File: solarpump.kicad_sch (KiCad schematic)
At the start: 16 parts, among them J1 8-way_Screw, J2 UART_IO, J3 AUX_POWER, J4 USB_A, J5 Conn_DISP, J6 Conn_DISP

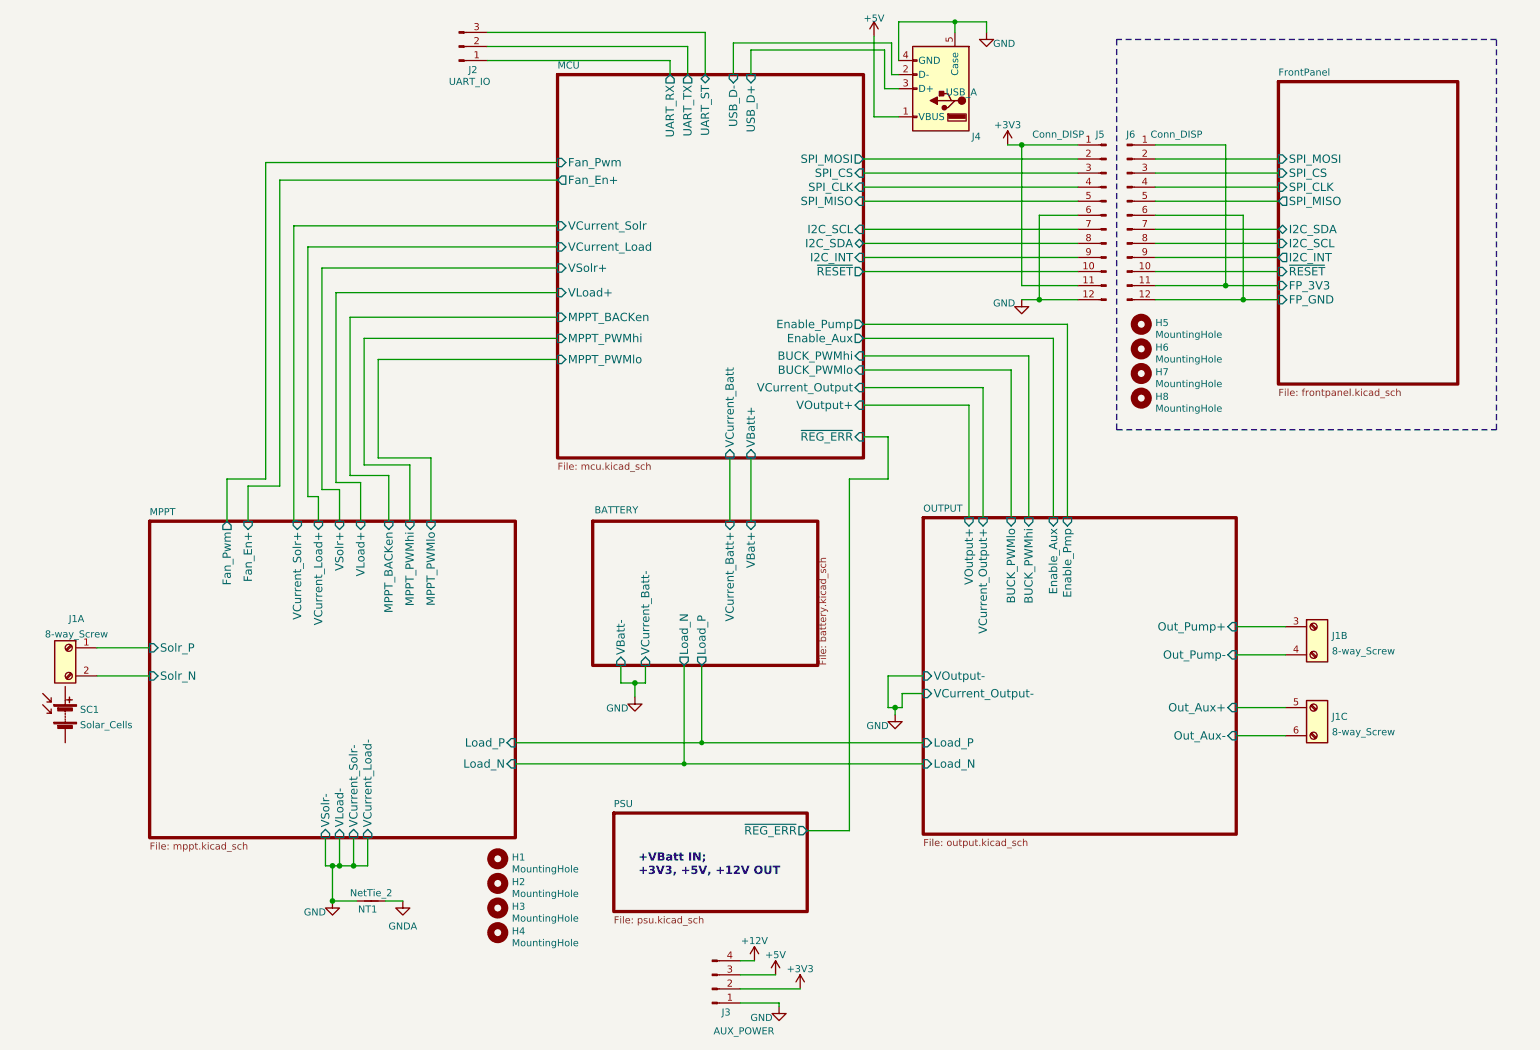
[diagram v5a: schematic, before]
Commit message: Rework with larger display; update component selection; add SWD conn; add RTC chip and QWIIC i2c socket
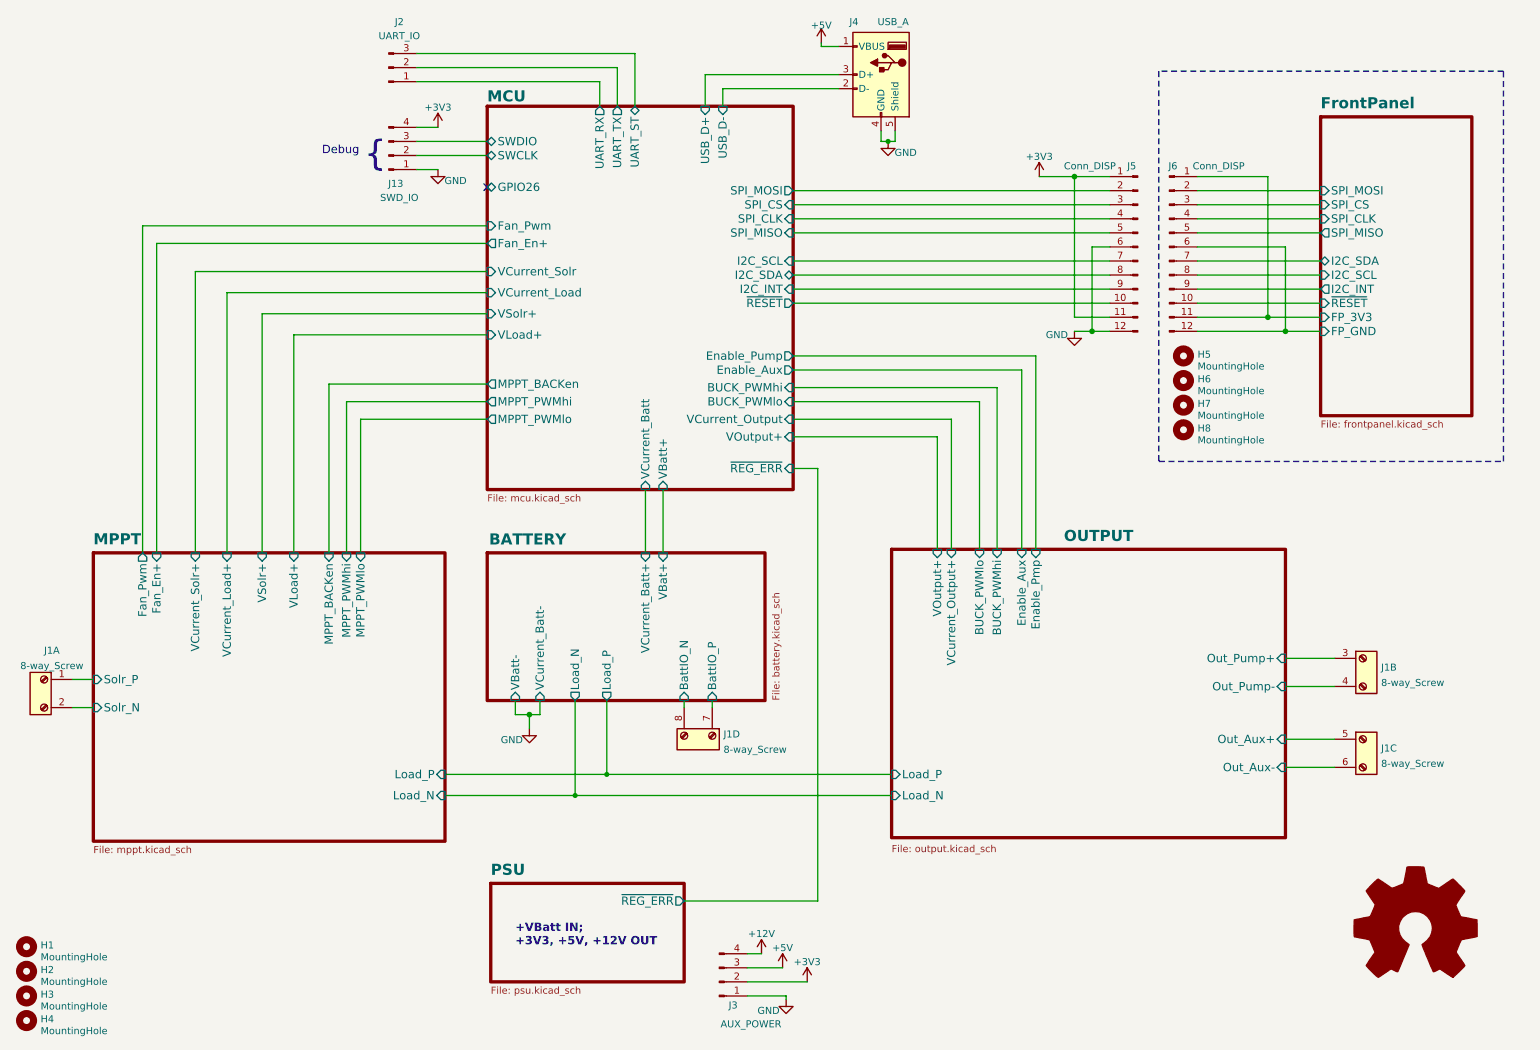
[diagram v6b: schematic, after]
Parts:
- removed NT1: NetTie_2, NetTie:NetTie-2_THT_Pad1.0mm, symbol Device:NetTie_2
- removed SC1: Solar_Cells, Connector_Wire:SolderWire-1.5sqmm_1x02_P6mm_D1.7mm_OD3mm, symbol Device:Solar_Cells
- added unit 4 of J1
- added J13: SWD_IO, Connector_PinHeader_2.00mm:PinHeader_1x04_P2.00mm_Vertical, symbol Connector:Conn_01x04_Male
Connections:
- net +3V3: now also J13.4 (Pin_4)
- net GND: now also J13.1 (Pin_1)
- new net BATTERY/BattIO_N: J1.8 (Pin_8)
- new net BATTERY/BattIO_P: J1.7 (Pin_7)
- new net MCU/SWCLK: J13.2 (Pin_2)
- new net MCU/SWDIO: J13.3 (Pin_3)
- no-connect marks 0 -> 1
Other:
- sheet BATTERY ports: added BattIO_N, BattIO_P; removed none
- sheet MCU ports: added GPIO26, SWCLK, SWDIO; removed none
- sheet MPPT ports: added none; removed VCurrent_Load-, VCurrent_Solr-, VLoad-, VSolr-
- sheet OUTPUT ports: added none; removed VCurrent_Output-, VOutput-
- note added: "Debug"
- note added: "{"
- moved on the sheet: H1, H2, H3, H4, H5, H6, H7, H8, J1A, J1B, J1C, J2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

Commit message: More updates to regularise property names
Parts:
- J1: Manuf (none) -> Phoenix Contact; Mfr Phoenix Contact -> (none); Mfr Part No 1712708 -> (none); Part (none) -> 1712708; Supl Part No 651-1712708 -> (none); Supl Price 6.04 -> (none); Vendor Cost (none) -> 6.04; Vendor SKU (none) -> 651-1712708
- J13, J3: Manuf (none) -> Harwin; Mfr Harwin -> (none); Mfr Part No M22-2510405 -> (none); Part (none) -> M22-2510405; Supl Mouser -> (none); Supl Part No 855-M22-2510405 -> (none); Supl Price 0.26 -> (none); Vendor (none) -> Mouser; Vendor Cost (none) -> 0.26; Vendor SKU (none) -> 855-M22-2510405
- J2: Manuf (none) -> Harwin; Mfr Harwin -> (none); Mfr Part No M22-2510305 -> (none); Part (none) -> M22-2510305; Supl Mouser -> (none); Supl Part No 855-M22-2510305 -> (none); Supl Price 0.198 -> (none); Vendor (none) -> Mouser; Vendor Cost (none) -> 0.198; Vendor SKU (none) -> 855-M22-2510305
- J4: Manuf (none) -> GCT; Mfr GCT -> (none); Mfr Part No USB1040-GF-L-B -> (none); Part (none) -> USB1040-GF-L-B; Supl Mouser -> (none); Supl Part No 640-USB1040-GF-L-B -> (none); Supl Price 0.46 -> (none); Vendor (none) -> Mouser; Vendor Cost (none) -> 0.46; Vendor SKU (none) -> 640-USB1040-GF-L-B
- J5, J6: Manuf (none) -> TE Connectivity; Mfr TE Connectivity -> (none); Mfr Part No 2842126-6 -> (none); Part (none) -> 2842126-6; Supl Mouser -> (none); Supl Part No 571-2842126-6 -> (none); Supl Price 0.892 -> (none); Vendor (none) -> Mouser; Vendor Cost (none) -> 0.892; Vendor SKU (none) -> 571-2842126-6

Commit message: Fix some errors in the design (esp net-tie in wrong place)
 - correct led, diode footprints & model
 - fix fuse holder (bad hole spec)
 - update oled mod
 - update EC11 mod
 - add Blender models of case (xz compressed)
 - more updated gerbers (not current!)
 - improve layout of front panel pcb
 - delete unused files
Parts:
- J1: Vendor (none) -> Mouser
